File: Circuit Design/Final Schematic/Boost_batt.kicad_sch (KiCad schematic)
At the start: 0 parts

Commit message: Boost
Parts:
- added C_by, C_cv: 10n, Capacitor_SMD:C_0805_2012Metric_Pad1.18x1.45mm_HandSolder, symbol Device:C
- added C_by_2: C_Polarized, symbol Device:C_Polarized
- added Cby2: 0.1u, Capacitor_SMD:C_0805_2012Metric_Pad1.18x1.45mm_HandSolder, symbol Device:C
- added D?: 1N5819, Diode_THT:D_DO-41_SOD81_P10.16mm_Horizontal, symbol Diode:1N5819
- added Lb: L, symbol Device:L
- added Qb: IRF740, Package_TO_SOT_THT:TO-220-3_Vertical, symbol Transistor_FET:IRF740
- added Ra: 47, symbol Device:R
- added Rb: 100, Resistor_SMD:R_0805_2012Metric_Pad1.20x1.40mm_HandSolder, symbol Device:R
- added Ro: 1k, symbol Device:R
- added U_555: LM555xM, Package_SO:SOIC-8_3.9x4.9mm_P1.27mm, symbol Timer:LM555xM
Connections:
- net 5v0: now also C_by_2.1, D?.1 (K)
- net V_bat: now also Lb.1
- new net: C_by.2, Ra.1, Ro.1, U_555.4 (R), U_555.8 (VCC)
- new net: D?.2 (A), Qb.2 (D)
- new net: Ra.2, Rb.1, U_555.7 (DIS)
- new net: C_cv.1, U_555.5 (CV)
- new net GND: C_by.1, C_by_2.2, C_cv.2, Cby2.2, Qb.3 (S), U_555.1 (GND)
- new net PWM: Qb.1 (G), Ro.2, U_555.3 (Q)
- new net TT: Cby2.1, Rb.2, U_555.2 (TR), U_555.6 (THR)

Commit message: Footprints
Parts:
- C_by_2: footprint (none) -> Capacitor_SMD:CP_Elec_6.3x5.8
- Lb1: renamed from Lb; footprint (none) -> Inductor_THT:L_Toroid_Vertical_L25.4mm_W14.7mm_P12.20mm_Vishay_TJ5_BigPads
- Ra1: renamed from Ra; footprint (none) -> Resistor_SMD:R_0805_2012Metric_Pad1.20x1.40mm_HandSolder
- Ro1: renamed from Ro; footprint (none) -> Resistor_SMD:R_0805_2012Metric_Pad1.20x1.40mm_HandSolder
- gave numbers to parts that had none: 1
- renumbered C_by to C_by1, C_cv to C_cv1, Qb to Qb1, Rb to Rb1
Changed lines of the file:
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@@
   (symbol (lib_id "Device:R") (at 165.862 109.982 0) (unit 1)
     (in_bom yes) (on_board yes) (fields_autoplaced)
-    (property "Reference" "Ro" (id 0) (at 168.402 108.7119 0)
+    (property "Reference" "Ro1" (id 0) (at 168.402 108.7119 0)
       (effects (font (size 1.27 1.27)) (justify left))
     )
@@
       (effects (font (size 1.27 1.27)) (justify left))
     )
-    (property "Footprint" "" (id 2) (at 164.084 109.982 90)
+    (property "Footprint" "Resistor_SMD:R_0805_2012Metric_Pad1.20x1.40mm_HandSolder" (id 2) (at 164.084 109.982 90)
       (effects (font (size 1.27 1.27)) hide)
     )
@@
   (symbol (lib_id "power:GND") (at 134.112 103.632 270) (unit 1)
     (in_bom yes) (on_board yes)
-    (property "Reference" "#PWR?" (id 0) (at 127.762 103.632 0)
+    (property "Reference" "#PWR0161" (id 0) (at 127.762 103.632 0)
       (effects (font (size 1.27 1.27)) hide)
     )
@@
   (symbol (lib_id "Diode:1N5819") (at 156.337 62.23 180) (unit 1)
     (in_bom yes) (on_board yes) (fields_autoplaced)
-    (property "Reference" "D?" (id 0) (at 156.6545 55.245 0))
-    (property "Value" "1N5819" (id 1) (at 156.6545 57.785 0))
+    (property "Reference" "DBoo1" (id 0) (at 156.6545 55.88 0))
+    (property "Value" "1N5819" (id 1) (at 156.6545 58.42 0))
     (property "Footprint" "Diode_THT:D_DO-41_SOD81_P10.16mm_Horizontal" (id 2) (at 156.337 57.785 0)
       (effects (font (size 1.27 1.27)) hide)
@@
   (symbol (lib_id "Device:R") (at 176.022 126.492 0) (unit 1)
     (in_bom yes) (on_board yes) (fields_autoplaced)
-    (property "Reference" "Rb" (id 0) (at 177.927 125.2219 0)
+    (property "Reference" "Rb1" (id 0) (at 177.927 125.2219 0)
       (effects (font (size 1.27 1.27)) (justify left))
     )
@@
   (symbol (lib_id "power:GND") (at 151.892 131.572 0) (unit 1)
     (in_bom yes) (on_board yes) (fields_autoplaced)
-    (property "Reference" "#PWR?" (id 0) (at 151.892 137.922 0)
+    (property "Reference" "#PWR0158" (id 0) (at 151.892 137.922 0)
       (effects (font (size 1.27 1.27)) hide)
     )
@@
   (symbol (lib_id "Device:L") (at 133.477 62.357 90) (unit 1)
     (in_bom yes) (on_board yes) (fields_autoplaced)
-    (property "Reference" "Lb" (id 0) (at 133.477 56.642 90))
+    (property "Reference" "Lb1" (id 0) (at 133.477 56.642 90))
     (property "Value" "L" (id 1) (at 133.477 59.182 90))
-    (property "Footprint" "" (id 2) (at 133.477 62.357 0)
+    (property "Footprint" "Inductor_THT:L_Toroid_Vertical_L25.4mm_W14.7mm_P12.20mm_Vishay_TJ5_BigPads" (id 2) (at 133.477 62.357 0)
       (effects (font (size 1.27 1.27)) hide)
     )
@@
   (symbol (lib_id "Device:C") (at 139.827 103.632 90) (unit 1)
     (in_bom yes) (on_board yes)
-    (property "Reference" "C_by" (id 0) (at 141.859 110.1091 90)
+    (property "Reference" "C_by1" (id 0) (at 141.859 110.1091 90)
       (effects (font (size 1.27 1.27)) (justify left))
     )
@@
       (effects (font (size 1.27 1.27)) (justify left))
     )
-    (property "Footprint" "" (id 2) (at 169.3672 74.93 0)
+    (property "Footprint" "Capacitor_SMD:CP_Elec_6.3x5.8" (id 2) (at 169.3672 74.93 0)
       (effects (font (size 1.27 1.27)) hide)
     )
@@
   (symbol (lib_id "Device:C") (at 130.937 126.492 0) (unit 1)
     (in_bom yes) (on_board yes) (fields_autoplaced)
-    (property "Reference" "C_cv" (id 0) (at 134.112 125.2219 0)
+    (property "Reference" "C_cv1" (id 0) (at 134.112 125.2219 0)
       (effects (font (size 1.27 1.27)) (justify left))
     )
@@
   (symbol (lib_id "power:GND") (at 176.022 141.097 0) (unit 1)
     (in_bom yes) (on_board yes) (fields_autoplaced)
-    (property "Reference" "#PWR?" (id 0) (at 176.022 147.447 0)
+    (property "Reference" "#PWR0157" (id 0) (at 176.022 147.447 0)
       (effects (font (size 1.27 1.27)) hide)
     )
@@
   (symbol (lib_id "Device:R") (at 176.022 116.967 0) (unit 1)
     (in_bom yes) (on_board yes) (fields_autoplaced)
-    (property "Reference" "Ra" (id 0) (at 177.927 115.6969 0)
+    (property "Reference" "Ra1" (id 0) (at 177.927 115.6969 0)
       (effects (font (size 1.27 1.27)) (justify left))
     )
@@
       (effects (font (size 1.27 1.27)) (justify left))
     )
-    (property "Footprint" "" (id 2) (at 174.244 116.967 90)
+    (property "Footprint" "Resistor_SMD:R_0805_2012Metric_Pad1.20x1.40mm_HandSolder" (id 2) (at 174.244 116.967 90)
       (effects (font (size 1.27 1.27)) hide)
     )
@@
   (symbol (lib_id "power:GND") (at 168.402 77.47 0) (unit 1)
     (in_bom yes) (on_board yes) (fields_autoplaced)
-    (property "Reference" "#PWR?" (id 0) (at 168.402 83.82 0)
+    (property "Reference" "#PWR0160" (id 0) (at 168.402 83.82 0)
       (effects (font (size 1.27 1.27)) hide)
     )
@@
   (symbol (lib_id "power:GND") (at 130.937 131.572 0) (unit 1)
     (in_bom yes) (on_board yes) (fields_autoplaced)
-    (property "Reference" "#PWR?" (id 0) (at 130.937 137.922 0)
+    (property "Reference" "#PWR0159" (id 0) (at 130.937 137.922 0)
       (effects (font (size 1.27 1.27)) hide)
     )
@@
   (symbol (lib_id "Transistor_FET:IRF740") (at 141.732 71.12 0) (unit 1)
     (in_bom yes) (on_board yes) (fields_autoplaced)
-    (property "Reference" "Qb" (id 0) (at 148.082 69.8499 0)
+    (property "Reference" "Qb1" (id 0) (at 148.082 69.8499 0)
       (effects (font (size 1.27 1.27)) (justify left))
     )
@@
   (symbol (lib_id "power:GND") (at 144.272 76.2 0) (unit 1)
     (in_bom yes) (on_board yes) (fields_autoplaced)
-    (property "Reference" "#PWR?" (id 0) (at 144.272 82.55 0)
-      (effects (font (size 1.27 1.27)) hide)
-    )
+    (property "Reference" "#PWR0162" (id 0) (at 144.272 82.55 0)
+      (effects (font (size 1.27 1.27)) hide)
+    )

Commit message: Organización PCB
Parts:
- Lb1: value L -> 100u
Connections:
- net at DBoo1.2 (A), Qb1.2 (D): now also Lb1.2
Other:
- moved on the sheet: Lb1
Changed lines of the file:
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@@
   (junction (at 152.019 103.759) (diameter 0) (color 0 0 0 0)
   )
+  (junction (at 144.272 62.23) (diameter 0) (color 0 0 0 0)
+  )
   (junction (at 176.022 121.412) (diameter 0) (color 0 0 0 0)
   )
@@
   (junction (at 151.892 109.982) (diameter 0) (color 0 0 0 0)
   )
-  (junction (at 144.272 62.23) (diameter 0) (color 0 0 0 0)
-  )
   (junction (at 165.862 116.332) (diameter 0) (color 0 0 0 0)
   )
   (junction (at 168.402 62.23) (diameter 0) (color 0 0 0 0)
   )
-  (junction (at 137.287 62.357) (diameter 0) (color 0 0 0 0)
-  )
   (wire (pts (xy 135.382 116.332) (xy 139.192 116.332))
     (stroke (width 0) (type default) (color 0 0 0 0))
@@
     (stroke (width 0) (type default) (color 0 0 0 0))
   )
+  (wire (pts (xy 135.89 62.23) (xy 144.272 62.23))
+    (stroke (width 0) (type default) (color 0 0 0 0))
+  )
+  (wire (pts (xy 124.46 62.23) (xy 128.27 62.23))
+    (stroke (width 0) (type default) (color 0 0 0 0))
+  )
+  (wire (pts (xy 143.637 103.632) (xy 151.892 103.632))
+    (stroke (width 0) (type default) (color 0 0 0 0))
+  )
+  (wire (pts (xy 168.402 74.93) (xy 168.402 77.47))
+    (stroke (width 0) (type default) (color 0 0 0 0))
+  )
+  (wire (pts (xy 168.402 62.23) (xy 168.402 67.31))
+    (stroke (width 0) (type default) (color 0 0 0 0))
+  )
+  (wire (pts (xy 148.717 113.157) (xy 148.717 109.982))
+    (stroke (width 0) (type default) (color 0 0 0 0))
+  )
+  (wire (pts (xy 164.592 116.332) (xy 165.862 116.332))
+    (stroke (width 0) (type default) (color 0 0 0 0))
+  )
+  (wire (pts (xy 139.192 123.317) (xy 142.367 123.317))
+    (stroke (width 0) (type default) (color 0 0 0 0))
+  )
+  (wire (pts (xy 130.937 130.302) (xy 130.937 131.572))
+    (stroke (width 0) (type default) (color 0 0 0 0))
+  )
+  (wire (pts (xy 164.592 121.412) (xy 176.022 121.412))
+    (stroke (width 0) (type default) (color 0 0 0 0))
+  )
+  (wire (pts (xy 168.402 62.23) (xy 187.452 62.23))
+    (stroke (width 0) (type default) (color 0 0 0 0))
+  )
+  (wire (pts (xy 151.892 103.632) (xy 165.862 103.632))
+    (stroke (width 0) (type default) (color 0 0 0 0))
+  )
+  (wire (pts (xy 151.892 109.982) (xy 151.892 111.252))
+    (stroke (width 0) (type default) (color 0 0 0 0))
+  )
+  (wire (pts (xy 139.192 126.492) (xy 139.192 123.317))
+    (stroke (width 0) (type default) (color 0 0 0 0))
+  )
+  (wire (pts (xy 165.862 116.332) (xy 167.132 116.332))
+    (stroke (width 0) (type default) (color 0 0 0 0))
+  )
+  (wire (pts (xy 176.022 131.572) (xy 176.022 132.207))
+    (stroke (width 0) (type default) (color 0 0 0 0))
+  )
+  (wire (pts (xy 165.862 113.792) (xy 165.862 116.332))
+    (stroke (width 0) (type default) (color 0 0 0 0))
+  )
+  (wire (pts (xy 142.367 123.317) (xy 142.367 113.157))
+    (stroke (width 0) (type default) (color 0 0 0 0))
+  )
   (wire (pts (xy 144.272 62.23) (xy 152.527 62.23))
-    (stroke (width 0) (type default) (color 0 0 0 0))
-  )
-  (wire (pts (xy 127.381 62.357) (xy 129.667 62.357))
-    (stroke (width 0) (type default) (color 0 0 0 0))
-  )
-  (wire (pts (xy 143.637 103.632) (xy 151.892 103.632))
-    (stroke (width 0) (type default) (color 0 0 0 0))
-  )
-  (wire (pts (xy 168.402 74.93) (xy 168.402 77.47))
-    (stroke (width 0) (type default) (color 0 0 0 0))
-  )
-  (wire (pts (xy 168.402 62.23) (xy 168.402 67.31))
-    (stroke (width 0) (type default) (color 0 0 0 0))
-  )
-  (wire (pts (xy 137.287 62.23) (xy 144.272 62.23))
-    (stroke (width 0) (type default) (color 0 0 0 0))
-  )
-  (wire (pts (xy 148.717 113.157) (xy 148.717 109.982))
-    (stroke (width 0) (type default) (color 0 0 0 0))
-  )
-  (wire (pts (xy 164.592 116.332) (xy 165.862 116.332))
-    (stroke (width 0) (type default) (color 0 0 0 0))
-  )
-  (wire (pts (xy 139.192 123.317) (xy 142.367 123.317))
-    (stroke (width 0) (type default) (color 0 0 0 0))
-  )
-  (wire (pts (xy 130.937 130.302) (xy 130.937 131.572))
-    (stroke (width 0) (type default) (color 0 0 0 0))
-  )
-  (wire (pts (xy 164.592 121.412) (xy 176.022 121.412))
-    (stroke (width 0) (type default) (color 0 0 0 0))
-  )
-  (wire (pts (xy 168.402 62.23) (xy 187.452 62.23))
-    (stroke (width 0) (type default) (color 0 0 0 0))
-  )
-  (wire (pts (xy 151.892 103.632) (xy 165.862 103.632))
-    (stroke (width 0) (type default) (color 0 0 0 0))
-  )
-  (wire (pts (xy 151.892 109.982) (xy 151.892 111.252))
-    (stroke (width 0) (type default) (color 0 0 0 0))
-  )
-  (wire (pts (xy 139.192 126.492) (xy 139.192 123.317))
-    (stroke (width 0) (type default) (color 0 0 0 0))
-  )
-  (wire (pts (xy 165.862 116.332) (xy 167.132 116.332))
-    (stroke (width 0) (type default) (color 0 0 0 0))
-  )
-  (wire (pts (xy 176.022 131.572) (xy 176.022 132.207))
-    (stroke (width 0) (type default) (color 0 0 0 0))
-  )
-  (wire (pts (xy 165.862 113.792) (xy 165.862 116.332))
-    (stroke (width 0) (type default) (color 0 0 0 0))
-  )
-  (wire (pts (xy 142.367 123.317) (xy 142.367 113.157))
     (stroke (width 0) (type default) (color 0 0 0 0))
   )
@@
     (effects (font (size 1.27 1.27)) (justify left bottom))
   )
-  (hierarchical_label "V_bat" (shape input) (at 127.381 62.357 180)
+  (hierarchical_label "V_bat" (shape input) (at 124.46 62.23 180)
     (effects (font (size 1.27 1.27)) (justify right))
   )
@@
     (pin "7")
   )
-  (symbol (lib_id "Device:L") (at 133.477 62.357 90) (unit 1)
-    (in_bom yes) (on_board yes) (fields_autoplaced)
-    (property "Reference" "Lb1" (id 0) (at 133.477 56.642 90))
-    (property "Value" "L" (id 1) (at 133.477 59.182 90))
-    (property "Footprint" "Inductor_THT:L_Toroid_Vertical_L25.4mm_W14.7mm_P12.20mm_Vishay_TJ5_BigPads" (id 2) (at 133.477 62.357 0)
-      (effects (font (size 1.27 1.27)) hide)
-    )
-    (property "Datasheet" "~" (id 3) (at 133.477 62.357 0)
-      (effects (font (size 1.27 1.27)) hide)
-    )
+  (symbol (lib_id "Device:L") (at 132.08 62.23 90) (unit 1)
+    (in_bom yes) (on_board yes) (fields_autoplaced)
+    (property "Reference" "Lb1" (id 0) (at 132.08 55.88 90))
+    (property "Value" "100u" (id 1) (at 132.08 58.42 90))
+    (property "Footprint" "Inductor_THT:L_Toroid_Vertical_L25.4mm_W14.7mm_P12.20mm_Vishay_TJ5_BigPads" (id 2) (at 132.08 62.23 0)
+      (effects (font (size 1.27 1.27)) hide)
+    )
+    (property "Datasheet" "~" (id 3) (at 132.08 62.23 0)
+      (effects (font (size 1.27 1.27)) hide)
+    )

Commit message: PCB distribution
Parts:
- DBoo1: footprint Diode_THT:D_DO-41_SOD81_P10.16mm_Horizontal -> Diode_THT:D_DO-201AE_P5.08mm_Vertical_AnodeUp
- renumbered C_by_2 to C_b1
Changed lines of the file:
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@@
     (property "Reference" "DBoo1" (id 0) (at 156.6545 55.88 0))
     (property "Value" "1N5819" (id 1) (at 156.6545 58.42 0))
-    (property "Footprint" "Diode_THT:D_DO-41_SOD81_P10.16mm_Horizontal" (id 2) (at 156.337 57.785 0)
+    (property "Footprint" "Diode_THT:D_DO-201AE_P5.08mm_Vertical_AnodeUp" (id 2) (at 156.337 57.785 0)
       (effects (font (size 1.27 1.27)) hide)
     )
@@
   (symbol (lib_id "Device:C_Polarized") (at 168.402 71.12 0) (unit 1)
     (in_bom yes) (on_board yes) (fields_autoplaced)
-    (property "Reference" "C_by_2" (id 0) (at 172.212 68.9609 0)
+    (property "Reference" "C_b1" (id 0) (at 172.212 68.9609 0)
       (effects (font (size 1.27 1.27)) (justify left))
     )

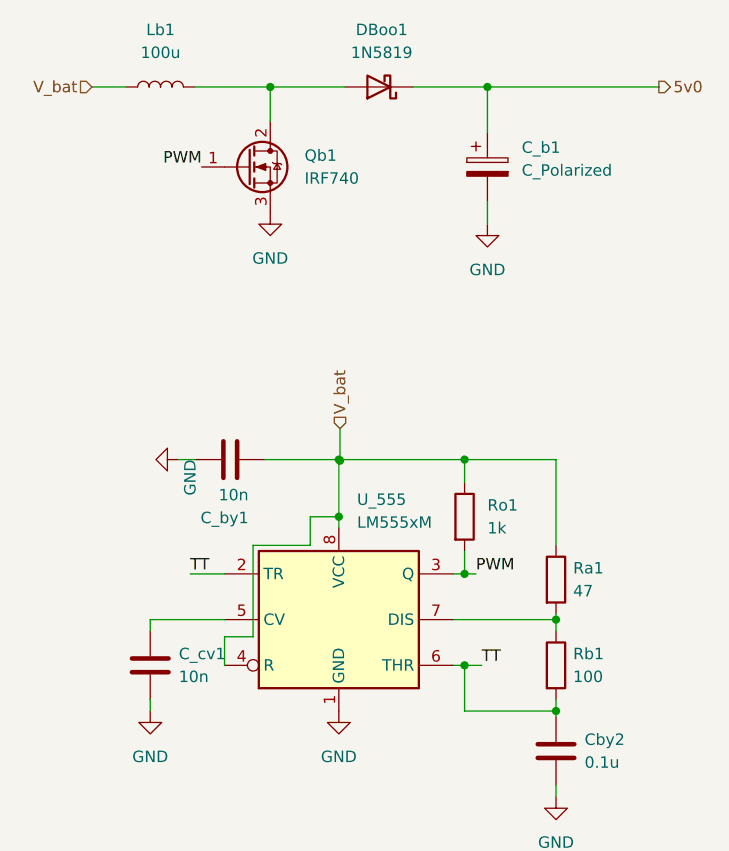
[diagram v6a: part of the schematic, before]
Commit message: Mounting holes
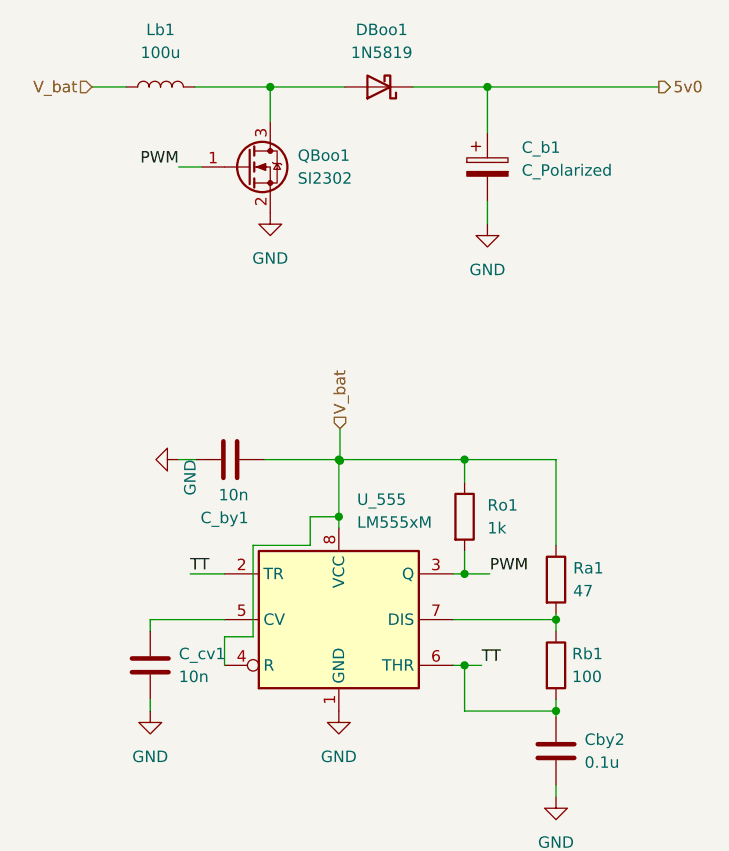
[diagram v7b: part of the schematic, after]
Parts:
- removed Qb1: IRF740, Package_TO_SOT_THT:TO-220-3_Vertical, symbol Transistor_FET:IRF740
- added QBoo1: SI2302, Package_TO_SOT_SMD:SOT-23, symbol Device:Q_NMOS_GSD
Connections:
- net GND: now also QBoo1.2 (S)
- net PWM: now also QBoo1.1 (G)
- net at DBoo1.2 (A), Lb1.2: now also QBoo1.3 (D)
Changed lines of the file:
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@@
+    (stroke (width 0) (type default) (color 0 0 0 0))
+  )
+  (wire (pts (xy 134.112 71.12) (xy 136.652 71.12))
     (stroke (width 0) (type default) (color 0 0 0 0))
   )
@@
     (stroke (width 0) (type default) (color 0 0 0 0))
   )
-  (wire (pts (xy 165.862 116.332) (xy 167.132 116.332))
+  (wire (pts (xy 165.862 116.332) (xy 168.656 116.332))
     (stroke (width 0) (type default) (color 0 0 0 0))
   )
@@
     (effects (font (size 1.27 1.27)) (justify left bottom))
   )
-  (label "PWM" (at 136.652 71.12 180)
+  (label "PWM" (at 134.112 71.12 180)
     (effects (font (size 1.27 1.27)) (justify right bottom))
   )
@@
     (effects (font (size 1.27 1.27)) (justify left bottom))
   )
-  (label "PWM" (at 167.132 116.332 0)
+  (label "PWM" (at 168.656 116.332 0)
     (effects (font (size 1.27 1.27)) (justify left bottom))
   )
@@
     (pin "2")
   )
+  (symbol (lib_id "Device:Q_NMOS_GSD") (at 141.732 71.12 0) (unit 1)
+    (in_bom yes) (on_board yes) (fields_autoplaced)
+    (property "Reference" "QBoo1" (id 0) (at 147.32 69.8499 0)
+      (effects (font (size 1.27 1.27)) (justify left))
+    )
+    (property "Value" "SI2302" (id 1) (at 147.32 72.3899 0)
+      (effects (font (size 1.27 1.27)) (justify left))
+    )
+    (property "Footprint" "Package_TO_SOT_SMD:SOT-23" (id 2) (at 146.812 68.58 0)
+      (effects (font (size 1.27 1.27)) hide)
+    )
+    (property "Datasheet" "~" (id 3) (at 141.732 71.12 0)
+      (effects (font (size 1.27 1.27)) hide)
+    )
+    (pin "1")
+    (pin "2")
+    (pin "3")
+  )
   (symbol (lib_id "Device:R") (at 176.022 126.492 0) (unit 1)
     (in_bom yes) (on_board yes) (fields_autoplaced)
-    (property "Reference" "Rb1" (id 0) (at 177.927 125.2219 0)
-      (effects (font (size 1.27 1.27)) (justify left))
-    )
-    (property "Value" "100" (id 1) (at 177.927 127.7619 0)
+    (property "Reference" "Rb1" (id 0) (at 177.8 125.2219 0)
+      (effects (font (size 1.27 1.27)) (justify left))
+    )
+    (property "Value" "100" (id 1) (at 177.8 127.7619 0)
       (effects (font (size 1.27 1.27)) (justify left))
     )
@@
     (pin "1")
   )
-  (symbol (lib_id "Transistor_FET:IRF740") (at 141.732 71.12 0) (unit 1)
-    (in_bom yes) (on_board yes) (fields_autoplaced)
-    (property "Reference" "Qb1" (id 0) (at 148.082 69.8499 0)
-      (effects (font (size 1.27 1.27)) (justify left))
-    )
-    (property "Value" "IRF740" (id 1) (at 148.082 72.3899 0)
-      (effects (font (size 1.27 1.27)) (justify left))
-    )
-    (property "Footprint" "Package_TO_SOT_THT:TO-220-3_Vertical" (id 2) (at 148.082 73.025 0)
-      (effects (font (size 1.27 1.27) italic) (justify left) hide)
-    )
-    (property "Datasheet" "http://www.vishay.com/docs/91054/91054.pdf" (id 3) (at 141.732 71.12 0)
-      (effects (font (size 1.27 1.27)) (justify left) hide)
-    )
-    (pin "1")
-    (pin "2")
-    (pin "3")
-  )
   (symbol (lib_id "power:GND") (at 144.272 76.2 0) (unit 1)
